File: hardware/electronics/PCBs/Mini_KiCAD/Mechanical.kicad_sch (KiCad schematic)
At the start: 32 parts

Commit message: Initial commit of the modified Ploopy Mini PCB with RP2040, PMW3360 and mid-mounted USB-C
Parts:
- removed FID1: IPC-7351 Fiducial 1mm, symbol Mini-altium-import:MCH_0_FIDUCIAL_1.5
- removed FID2: IPC-7351 Fiducial 1mm, FIDUCIAL_1.5, symbol Mini-altium-import:MCH_0_FIDUCIAL_1.5
- removed LOGO1: Ploopy logo, silkscreen, PloopyLogo, symbol Mini-altium-import:MCH_0_PloopyLogo
- removed LOGO2: Coordinate system marker for assembly, Coordinate System, symbol Mini-altium-import:MCH_0_CoordinateSystem
- MCH.SP.1, MCH.SP.10, MCH.SP.11, MCH.SP.12, MCH.SP.13, MCH.SP.14, MCH.SP.15, MCH.SP.16, MCH.SP.17, MCH.SP.18, MCH.SP.19, MCH.SP.2, MCH.SP.20, MCH.SP.21, MCH.SP.22, MCH.SP.23, MCH.SP.24, MCH.SP.25, MCH.SP.26, MCH.SP.27, MCH.SP.28, MCH.SP.3, MCH.SP.4, MCH.SP.5, MCH.SP.6, MCH.SP.7, MCH.SP.8, MCH.SP.9: footprint SparkGap -> PCBFeatures.PcbLib:SparkGap
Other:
- note removed: "${CURRENTTIME}"

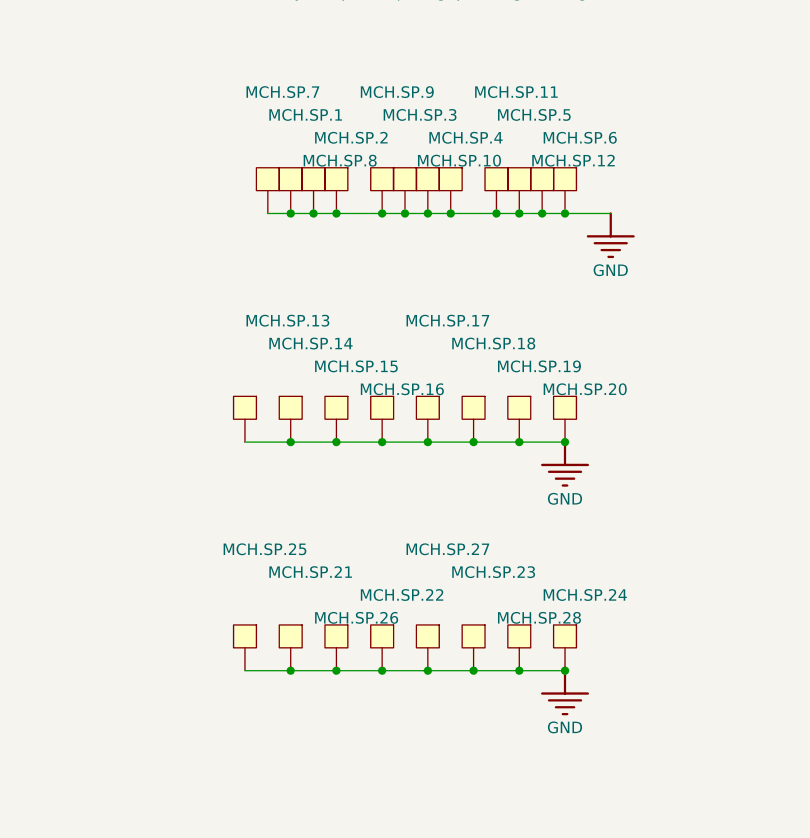
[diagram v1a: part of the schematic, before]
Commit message: Resolved most DRC errors and re-annotated the schematic to be friendly to BOM generation.
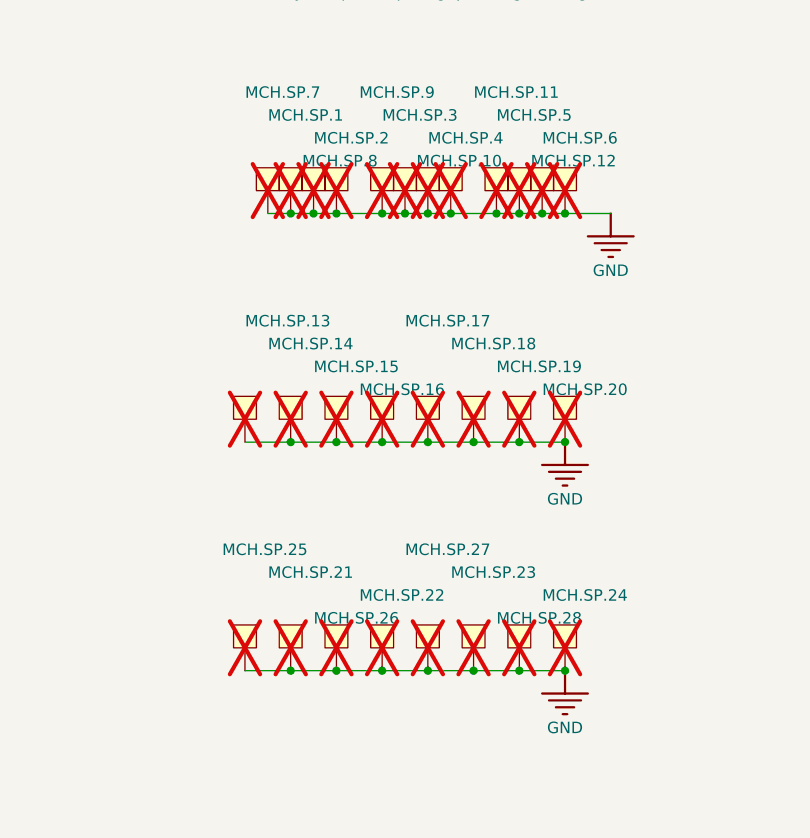
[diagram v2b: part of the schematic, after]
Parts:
- MCH.SP.1, MCH.SP.10, MCH.SP.11, MCH.SP.12, MCH.SP.13, MCH.SP.14, MCH.SP.15, MCH.SP.16, MCH.SP.17, MCH.SP.18, MCH.SP.19, MCH.SP.2, MCH.SP.20, MCH.SP.21, MCH.SP.22, MCH.SP.23, MCH.SP.24, MCH.SP.25, MCH.SP.26, MCH.SP.27, MCH.SP.28, MCH.SP.3, MCH.SP.4, MCH.SP.5, MCH.SP.6, MCH.SP.7, MCH.SP.8, MCH.SP.9: now not fitted
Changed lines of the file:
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@@
 		(in_bom yes)
 		(on_board yes)
-		(dnp no)
+		(dnp yes)
 		(property "Reference" "MCH.SP.26"
 			(at 177.8 144.78 0)
@@
 		(in_bom yes)
 		(on_board yes)
-		(dnp no)
+		(dnp yes)
 		(property "Reference" "MCH.SP.5"
 			(at 198.12 88.9 0)
@@
 		(in_bom yes)
 		(on_board yes)
-		(dnp no)
+		(dnp yes)
 		(property "Reference" "MCH.SP.23"
 			(at 193.04 139.7 0)
@@
 		(in_bom yes)
 		(on_board yes)
-		(dnp no)
+		(dnp yes)
 		(property "Reference" "MCH.SP.28"
 			(at 198.12 144.78 0)
@@
 		(in_bom yes)
 		(on_board yes)
-		(dnp no)
+		(dnp yes)
 		(property "Reference" "MCH.SP.15"
 			(at 177.8 116.84 0)
@@
 		(in_bom yes)
 		(on_board yes)
-		(dnp no)
+		(dnp yes)
 		(property "Reference" "MCH.SP.8"
 			(at 176.53 93.98 0)
@@
 		(in_bom yes)
 		(on_board yes)
-		(dnp no)
+		(dnp yes)
 		(property "Reference" "MCH.SP.14"
 			(at 172.72 114.3 0)
@@
 		(in_bom yes)
 		(on_board yes)
-		(dnp no)
+		(dnp yes)
 		(property "Reference" "MCH.SP.19"
 			(at 198.12 116.84 0)
@@
 		(in_bom yes)
 		(on_board yes)
-		(dnp no)
+		(dnp yes)
 		(property "Reference" "MCH.SP.12"
 			(at 201.93 93.98 0)
@@
 		(in_bom yes)
 		(on_board yes)
-		(dnp no)
+		(dnp yes)
 		(property "Reference" "MCH.SP.2"
 			(at 177.8 91.44 0)
@@
 		(in_bom yes)
 		(on_board yes)
-		(dnp no)
+		(dnp yes)
 		(property "Reference" "MCH.SP.20"
 			(at 203.2 119.38 0)
@@
 		(in_bom yes)
 		(on_board yes)
-		(dnp no)
+		(dnp yes)
 		(property "Reference" "MCH.SP.3"
 			(at 185.42 88.9 0)
@@
 		(in_bom yes)
 		(on_board yes)
-		(dnp no)
+		(dnp yes)
 		(property "Reference" "MCH.SP.21"
 			(at 172.72 139.7 0)
@@
 		(in_bom yes)
 		(on_board yes)
-		(dnp no)
+		(dnp yes)
 		(property "Reference" "MCH.SP.24"
 			(at 203.2 142.24 0)
@@
 		(in_bom yes)
 		(on_board yes)
-		(dnp no)
+		(dnp yes)
 		(property "Reference" "MCH.SP.9"
 			(at 182.88 86.36 0)
@@
 		(in_bom yes)
 		(on_board yes)
-		(dnp no)
+		(dnp yes)
 		(property "Reference" "MCH.SP.6"
 			(at 203.2 91.44 0)
@@
 		(in_bom yes)
 		(on_board yes)
-		(dnp no)
+		(dnp yes)
 		(property "Reference" "MCH.SP.1"
 			(at 172.72 88.9 0)
@@
 		(in_bom yes)
 		(on_board yes)
-		(dnp no)
+		(dnp yes)
 		(property "Reference" "MCH.SP.4"
 			(at 190.5 91.44 0)
@@
 		(in_bom yes)
 		(on_board yes)
-		(dnp no)
+		(dnp yes)
 		(property "Reference" "MCH.SP.18"
 			(at 193.04 114.3 0)
@@
 		(in_bom yes)
 		(on_board yes)
-		(dnp no)
+		(dnp yes)
 		(property "Reference" "MCH.SP.13"
 			(at 170.18 111.76 0)
@@
 		(in_bom yes)
 		(on_board yes)
-		(dnp no)
+		(dnp yes)
 		(property "Reference" "MCH.SP.17"
 			(at 187.96 111.76 0)
@@
 		(in_bom yes)
 		(on_board yes)
-		(dnp no)
+		(dnp yes)
 		(property "Reference" "MCH.SP.27"
 			(at 187.96 137.16 0)
@@
 		(in_bom yes)
 		(on_board yes)
-		(dnp no)
+		(dnp yes)
 		(property "Reference" "MCH.SP.16"
 			(at 182.88 119.38 0)
@@
 		(in_bom yes)
 		(on_board yes)
-		(dnp no)
+		(dnp yes)
 		(property "Reference" "MCH.SP.7"
 			(at 170.18 86.36 0)
@@
 		(in_bom yes)
 		(on_board yes)
-		(dnp no)
+		(dnp yes)
 		(property "Reference" "MCH.SP.11"
 			(at 195.58 86.36 0)
@@
 		(in_bom yes)
 		(on_board yes)
-		(dnp no)
+		(dnp yes)
 		(property "Reference" "MCH.SP.25"
 			(at 167.64 137.16 0)
@@
 		(in_bom yes)
 		(on_board yes)
-		(dnp no)
+		(dnp yes)
 		(property "Reference" "MCH.SP.22"
 			(at 182.88 142.24 0)
@@
 		(in_bom yes)
 		(on_board yes)
-		(dnp no)
+		(dnp yes)
 		(property "Reference" "MCH.SP.10"
 			(at 189.23 93.98 0)

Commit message: Rev1.002 Replaced all symbols in the schematic with built-in symbols where applicable. Reoriented the sensor to solve interference and tracking issues. Replaced the mid-mount USB port with regular port.
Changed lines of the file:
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@@
 	)
 	(symbol
-		(lib_id "Mini-altium-import:GND_POWER_GROUND")
+		(lib_id "power:GND")
 		(at 210.82 99.06 0)
 		(unit 1)
@@
 			)
 		)
-		(property "Description" ""
+		(property "Description" "Power symbol creates a global label with name \"GND\" , ground"
 			(at 210.82 99.06 0)
 			(effects
@@
 			)
 		)
-		(pin ""
+		(pin "1"
 		)
 		(instances
@@
 	)
 	(symbol
-		(lib_id "Mini-altium-import:GND_POWER_GROUND")
+		(lib_id "power:GND")
 		(at 205.74 149.86 0)
 		(unit 1)
@@
 			)
 		)
-		(property "Description" ""
+		(property "Description" "Power symbol creates a global label with name \"GND\" , ground"
 			(at 205.74 149.86 0)
 			(effects
@@
 			)
 		)
-		(pin ""
+		(pin "1"
 		)
 		(instances
@@
 	)
 	(symbol
-		(lib_id "Mini-altium-import:GND_POWER_GROUND")
+		(lib_id "power:GND")
 		(at 205.74 124.46 0)
 		(unit 1)
@@
 			)
 		)
-		(property "Description" ""
+		(property "Description" "Power symbol creates a global label with name \"GND\" , ground"
 			(at 205.74 124.46 0)
 			(effects
@@
 			)
 		)
-		(pin ""
+		(pin "1"
 		)
 		(instances
